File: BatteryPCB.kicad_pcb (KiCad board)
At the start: 2 copper layers, 142 x 129.8 mm, 6 parts, among them J1 Pack1+, J2 Sense_Pack1, J3 Pack1-, J4 Sense_Pack2, J5 Pack2+, J6 Pack2-

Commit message: PCB is pretty much done, still need to tweak outline and silkscreen
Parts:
- added REF**: MountingHole_4.3mm_M4, Mounting_Holes:MountingHole_4.3mm_M4, F.Cu at (100.0, 104.0)
- added REF**: MountingHole_4.3mm_M4, Mounting_Holes:MountingHole_4.3mm_M4, F.Cu at (40.0, 104.0)
- added REF**: MountingHole_4.3mm_M4, Mounting_Holes:MountingHole_4.3mm_M4, F.Cu at (55.0, -14.0)
- added REF**: MountingHole_4.3mm_M4, Mounting_Holes:MountingHole_4.3mm_M4, F.Cu at (85.0, -14.0)
- moved J3 90.0 mm to (65.0, 90.0), turned to 180 degrees
- moved J4 12.2 mm to (70.0, 97.5)
- moved J2 2.68 mm to (30.0, 97.5)
- moved J1 0.50 mm to (13.0, 0.00)
- moved J6 0.50 mm to (127.0, 0.00)
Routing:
- added copper zone on F.Cu, net Net-(J3-Pad1)
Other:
- board size 142 x 129.8 mm -> 140 x 127 mm
- board text added: "CELL1"
- board text added: "CELL10"
- board text added: "CELL11"
- board text added: "CELL12"
- board text added: "CELL2"
- board text added: "CELL3"
- board text added: "CELL4"
- board text added: "CELL5"
- board text added: "CELL6"
- board text added: "CELL7"
- board text added: "CELL8"
- board text added: "CELL9"
- board text added: "NEGATIVE PACK 1 / POSITIVE PACK 2"
- board text added: "NEGATIVE PACK 2"
- board text added: "POSTIVE PACK 1"
- board text added: "SENSE"

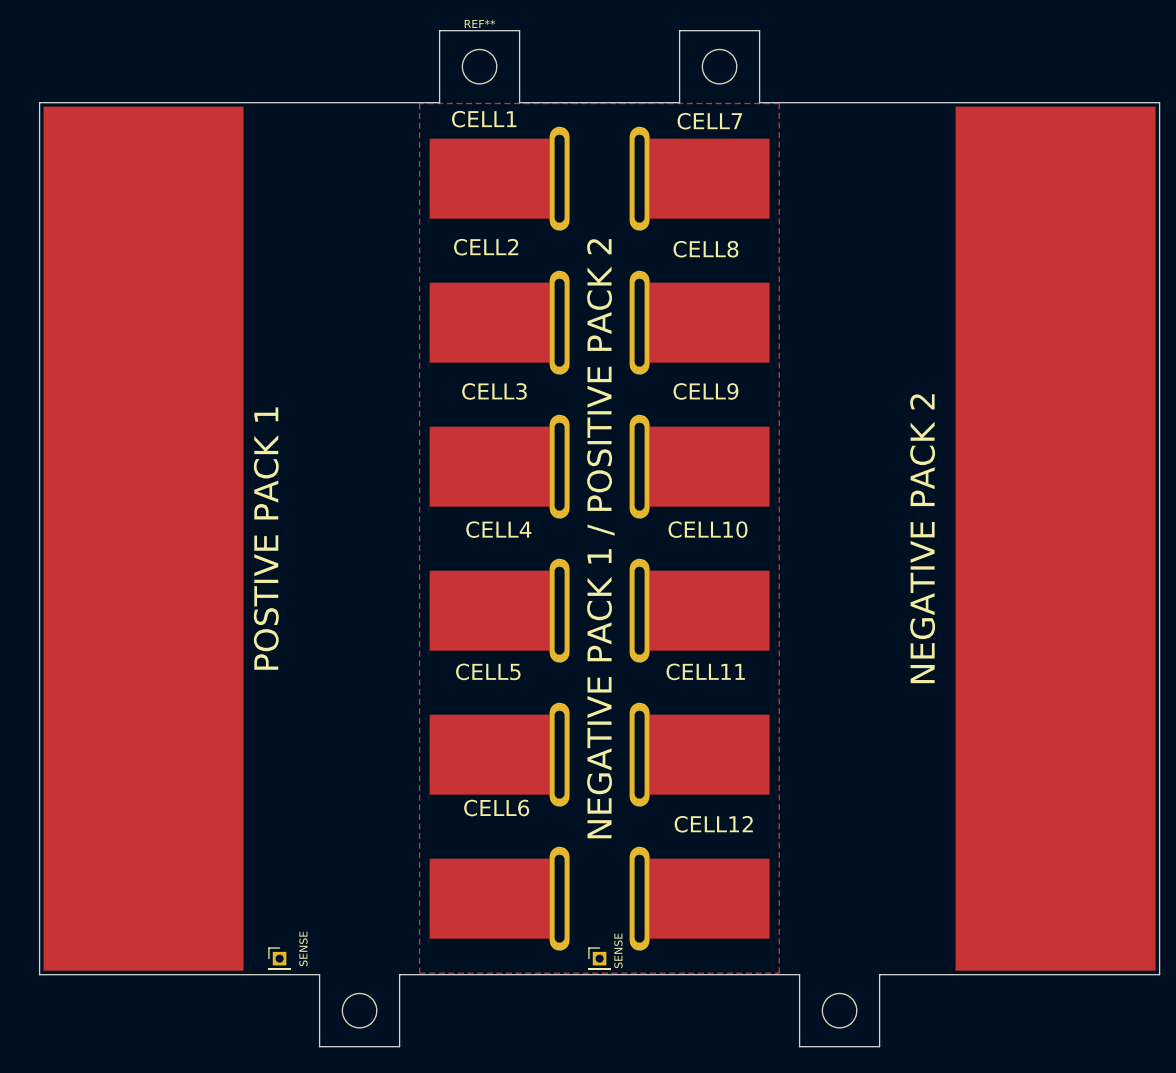
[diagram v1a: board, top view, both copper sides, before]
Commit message: finished the copper pours, worked on silkscreen
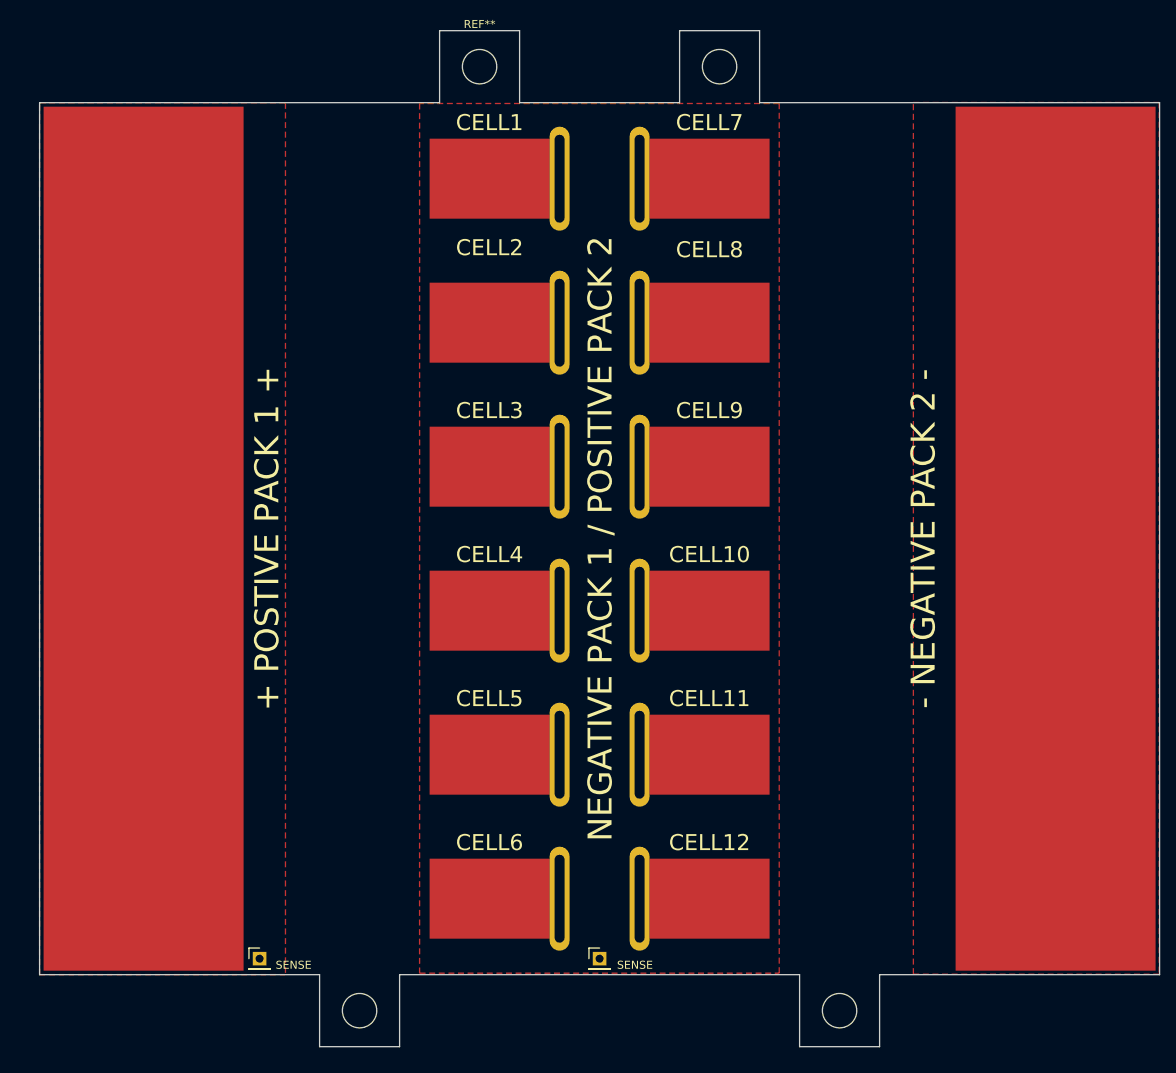
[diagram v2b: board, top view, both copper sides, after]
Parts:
- moved J2 2.50 mm to (27.5, 97.5)
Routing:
- added copper zone on F.Cu, net Net-(J1-Pad1)
- added copper zone on F.Cu, net Net-(J6-Pad1)
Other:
- board text added: "+ POSTIVE PACK 1 +"
- board text added: "- NEGATIVE PACK 2 -"
- board text removed: "NEGATIVE PACK 2"
- board text removed: "POSTIVE PACK 1"
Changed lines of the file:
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@@
   )
   (setup
-    (last_trace_width 0.25)
+    (last_trace_width 1)
+    (user_trace_width 1)
     (trace_clearance 0.2)
-    (zone_clearance 0.508)
+    (zone_clearance 0.254)
     (zone_45_only no)
     (trace_min 0.2)
@@
     (mod_text_size 1 1)
     (mod_text_width 0.15)
-    (pad_size 2.5 13)
-    (pad_drill 1.25)
+    (pad_size 15 10)
+    (pad_drill 0)
     (pad_to_mask_clearance 0.051)
     (solder_mask_min_width 0.25)
@@
   )
   (module Connector_PinHeader_2.54mm:PinHeader_1x01_P2.54mm_Vertical (layer F.Cu)
-    (at 30 97.5)
+    (at 27.5 97.5)
     (descr "Through hole straight pin header, 1x01, 2.54mm pitch, single row")
     (tags "Through hole pin header THT 1x01 2.54mm single row")
@@
       (net 1 "Net-(J1-Pad1)"))
   )
-  (gr_text SENSE (at 72.39 96.52 90) (layer F.SilkS)
+  (gr_text SENSE (at 74.422 98.298) (layer F.SilkS)
     (effects (font (size 1 1) (thickness 0.25)))
   )
-  (gr_text SENSE (at 33.02 96.266 90) (layer F.SilkS)
+  (gr_text SENSE (at 31.75 98.298) (layer F.SilkS)
     (effects (font (size 1 1) (thickness 0.25)))
   )
-  (gr_text "CELL12\n" (at 84.328 80.772) (layer F.SilkS)
-    (effects (font (size 2 2) (thickness 0.4)))
-  )
-  (gr_text CELL11 (at 83.312 61.722) (layer F.SilkS)
-    (effects (font (size 2 2) (thickness 0.4)))
-  )
-  (gr_text "CELL10\n" (at 83.566 43.942) (layer F.SilkS)
-    (effects (font (size 2 2) (thickness 0.4)))
-  )
-  (gr_text "CELL9\n" (at 83.312 26.67) (layer F.SilkS)
-    (effects (font (size 2 2) (thickness 0.4)))
-  )
-  (gr_text CELL8 (at 83.312 8.89) (layer F.SilkS)
-    (effects (font (size 2 2) (thickness 0.4)))
-  )
-  (gr_text "CELL7\n" (at 83.82 -7.112) (layer F.SilkS)
-    (effects (font (size 2 2) (thickness 0.4)))
-  )
-  (gr_text "CELL6\n" (at 57.15 78.74) (layer F.SilkS)
-    (effects (font (size 2 2) (thickness 0.4)))
-  )
-  (gr_text CELL5 (at 56.134 61.722) (layer F.SilkS)
-    (effects (font (size 2 2) (thickness 0.4)))
-  )
-  (gr_text CELL4 (at 57.404 43.942) (layer F.SilkS)
-    (effects (font (size 2 2) (thickness 0.4)))
-  )
-  (gr_text CELL3 (at 56.896 26.67) (layer F.SilkS)
-    (effects (font (size 2 2) (thickness 0.4)))
-  )
-  (gr_text CELL1 (at 55.626 -7.366) (layer F.SilkS)
-    (effects (font (size 2 2) (thickness 0.4)))
-  )
-  (gr_text "CELL2\n" (at 55.88 8.636) (layer F.SilkS)
-    (effects (font (size 2 2) (thickness 0.4)))
-  )
-  (gr_text "NEGATIVE PACK 2" (at 110.49 45 90) (layer F.SilkS)
+  (gr_text "CELL12\n" (at 83.75 83) (layer F.SilkS)
+    (effects (font (size 2 2) (thickness 0.4)))
+  )
+  (gr_text CELL11 (at 83.75 65) (layer F.SilkS)
+    (effects (font (size 2 2) (thickness 0.4)))
+  )
+  (gr_text "CELL10\n" (at 83.75 47) (layer F.SilkS)
+    (effects (font (size 2 2) (thickness 0.4)))
+  )
+  (gr_text "CELL9\n" (at 83.75 29) (layer F.SilkS)
+    (effects (font (size 2 2) (thickness 0.4)))
+  )
+  (gr_text CELL8 (at 83.75 8.89) (layer F.SilkS)
+    (effects (font (size 2 2) (thickness 0.4)))
+  )
+  (gr_text "CELL7\n" (at 83.75 -7) (layer F.SilkS)
+    (effects (font (size 2 2) (thickness 0.4)))
+  )
+  (gr_text "CELL6\n" (at 56.25 83) (layer F.SilkS)
+    (effects (font (size 2 2) (thickness 0.4)))
+  )
+  (gr_text CELL5 (at 56.25 65) (layer F.SilkS)
+    (effects (font (size 2 2) (thickness 0.4)))
+  )
+  (gr_text CELL4 (at 56.25 47) (layer F.SilkS)
+    (effects (font (size 2 2) (thickness 0.4)))
+  )
+  (gr_text CELL3 (at 56.25 29) (layer F.SilkS)
+    (effects (font (size 2 2) (thickness 0.4)))
+  )
+  (gr_text CELL1 (at 56.25 -7) (layer F.SilkS)
+    (effects (font (size 2 2) (thickness 0.4)))
+  )
+  (gr_text "CELL2\n" (at 56.25 8.636) (layer F.SilkS)
+    (effects (font (size 2 2) (thickness 0.4)))
+  )
+  (gr_text "- NEGATIVE PACK 2 -" (at 110.49 45 90) (layer F.SilkS)
     (effects (font (size 3 3) (thickness 0.5)))
   )
@@
     (effects (font (size 3 3) (thickness 0.5)))
   )
-  (gr_text "POSTIVE PACK 1" (at 28.448 45 90) (layer F.SilkS)
+  (gr_text "+ POSTIVE PACK 1 +" (at 28.448 45 90) (layer F.SilkS)
     (effects (font (size 3 3) (thickness 0.5)))
   )
@@
       )
     )
+  )
+  (zone (net 3) (net_name "Net-(J6-Pad1)") (layer F.Cu) (hatch edge 0.508)
+    (connect_pads yes (clearance 0.254))
+    (min_thickness 0.254)
+    (fill yes (arc_segments 32) (thermal_gap 0.508) (thermal_bridge_width 0.508))
+    (polygon
+      (pts
+        (xy 139.954 99.441) (xy 109.22 99.441) (xy 109.22 -9.525) (xy 139.954 -9.525)
+      )
+    )
+  )
+  (zone (net 1) (net_name "Net-(J1-Pad1)") (layer F.Cu) (hatch edge 0.508)
+    (connect_pads yes (clearance 0.254))
+    (min_thickness 0.254)
+    (fill yes (arc_segments 32) (thermal_gap 0.508) (thermal_bridge_width 0.508))
+    (polygon
+      (pts
+        (xy 30.734 99.48943) (xy 0 99.48943) (xy 0 -9.47657) (xy 30.734 -9.47657)
+      )
+    )
